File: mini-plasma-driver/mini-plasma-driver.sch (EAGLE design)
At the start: 73 parts, among them IC1 IR21844D, IC2 74LS19N, IC3 NE555N, IC4 NCP781IC, IC5 IR21844D, Q1 IRF640, Q2 IRF640, Q3 2N2369, Q4 2N2369, Q5 IRF640, Q6 IRF640

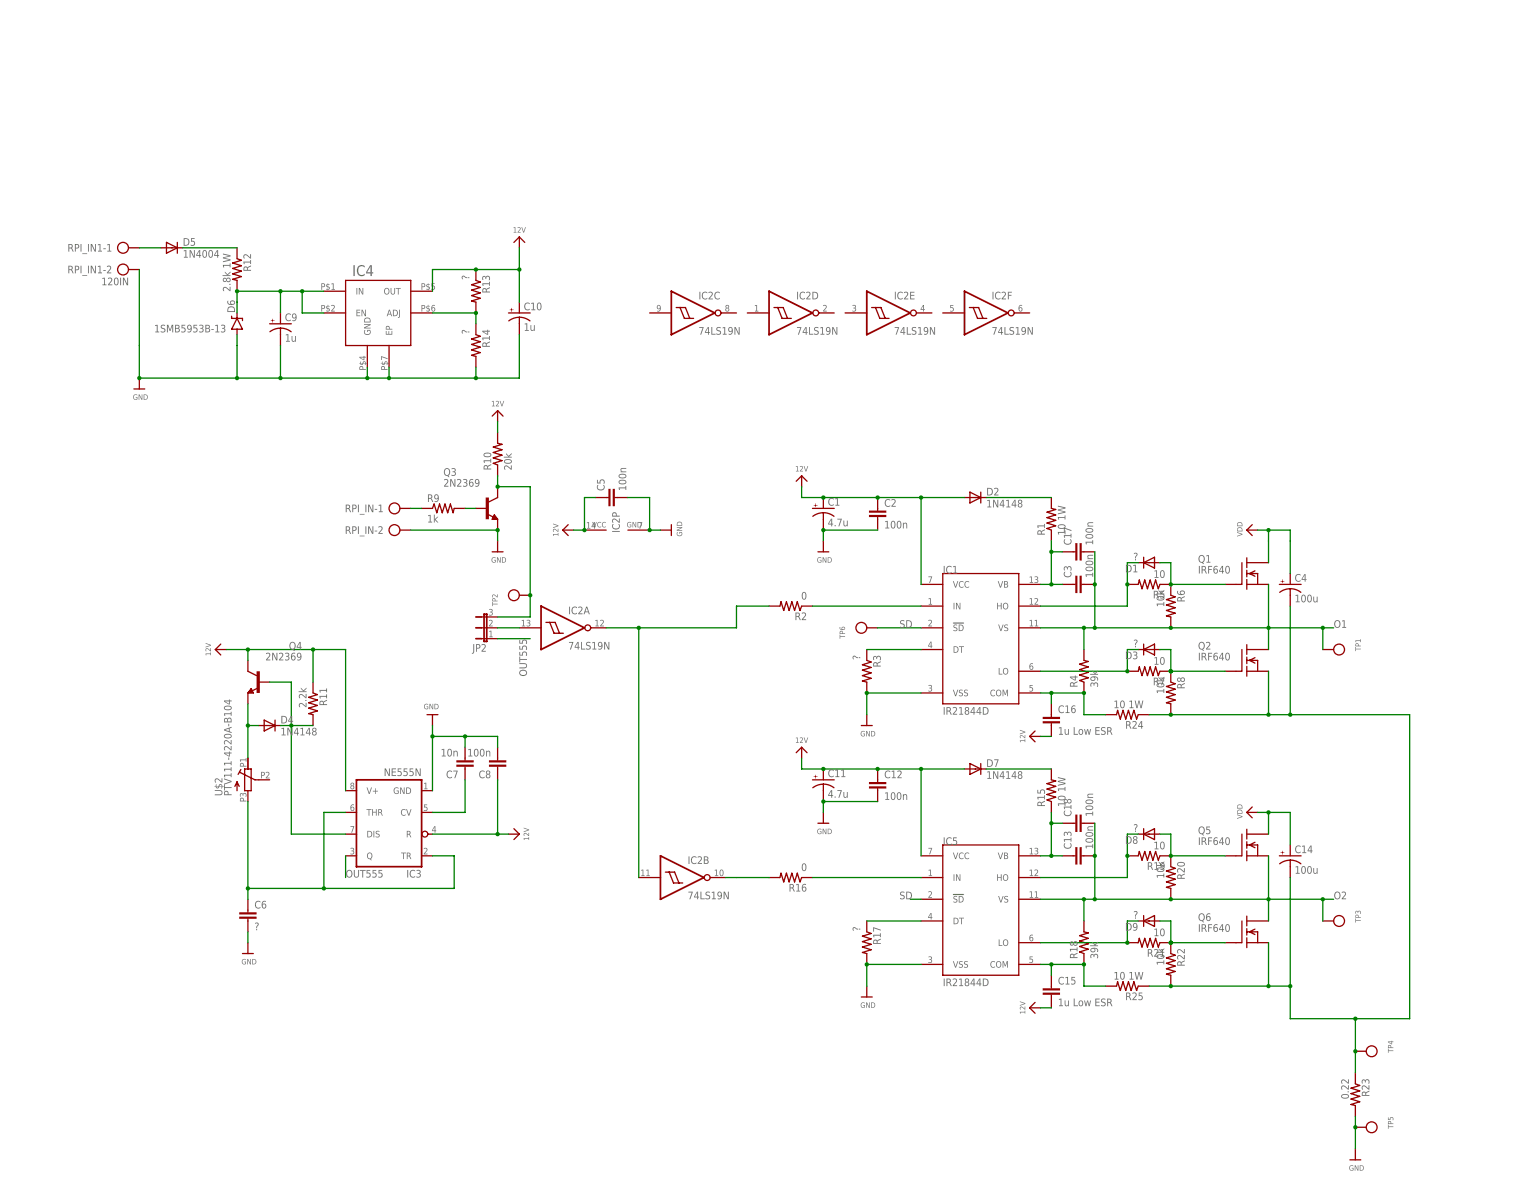
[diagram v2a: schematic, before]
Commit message: changed labels on AC connector and on 4 diodes
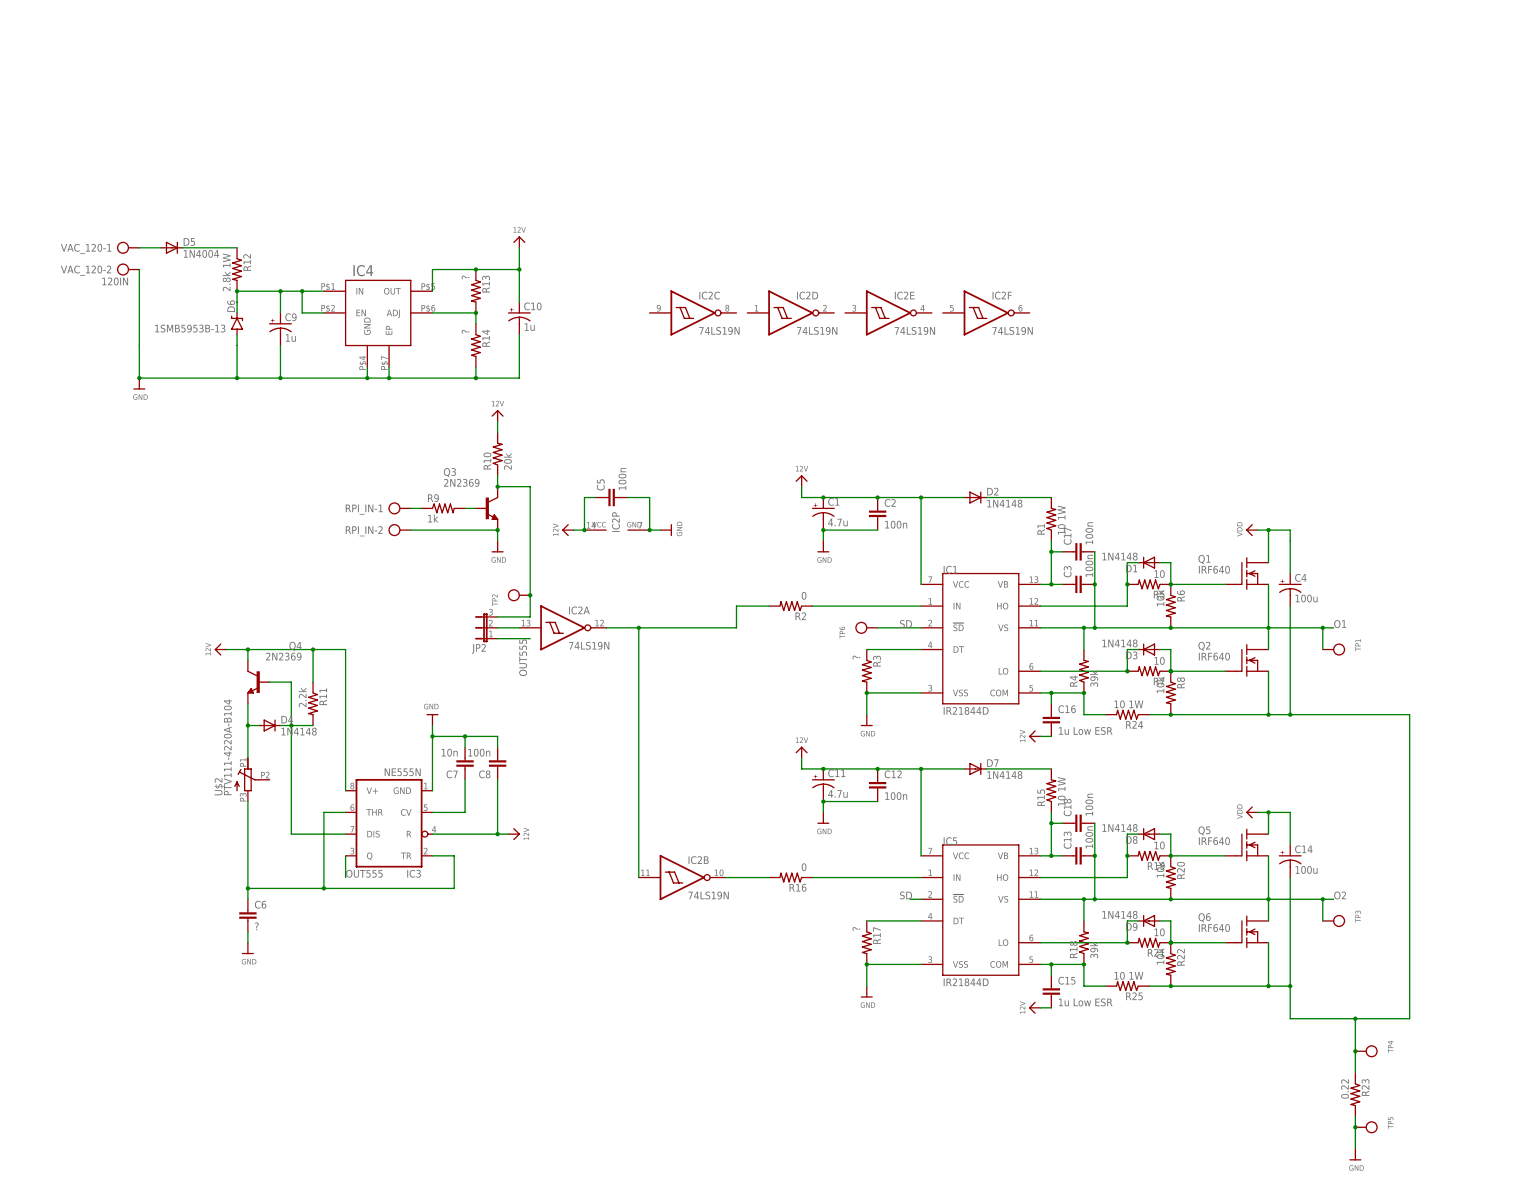
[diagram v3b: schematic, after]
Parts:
- D1, D3, D8, D9: value ? -> 1N4148
- renumbered RPI_IN1 to VAC_120
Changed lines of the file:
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@@
 <part name="R4" library="rcl" library_urn="urn:adsk.eagle:library:334" deviceset="R-US_" device="0207/10" package3d_urn="urn:adsk.eagle:package:23491/1" value="39k"/>
 <part name="D2" library="diode" library_urn="urn:adsk.eagle:library:210" deviceset="1N4148" device="DO35-10" package3d_urn="urn:adsk.eagle:package:43344/2" value="1N4148"/>
-<part name="D1" library="diode" library_urn="urn:adsk.eagle:library:210" deviceset="1N4148" device="DO35-10" package3d_urn="urn:adsk.eagle:package:43344/2" value="?"/>
+<part name="D1" library="diode" library_urn="urn:adsk.eagle:library:210" deviceset="1N4148" device="DO35-10" package3d_urn="urn:adsk.eagle:package:43344/2" value="1N4148"/>
 <part name="R5" library="rcl" library_urn="urn:adsk.eagle:library:334" deviceset="R-US_" device="0207/10" package3d_urn="urn:adsk.eagle:package:23491/1" value="10"/>
 <part name="R6" library="rcl" library_urn="urn:adsk.eagle:library:334" deviceset="R-US_" device="0207/10" package3d_urn="urn:adsk.eagle:package:23491/1" value="10k"/>
-<part name="D3" library="diode" library_urn="urn:adsk.eagle:library:210" deviceset="1N4148" device="DO35-10" package3d_urn="urn:adsk.eagle:package:43344/2" value="?"/>
+<part name="D3" library="diode" library_urn="urn:adsk.eagle:library:210" deviceset="1N4148" device="DO35-10" package3d_urn="urn:adsk.eagle:package:43344/2" value="1N4148"/>
 <part name="R7" library="rcl" library_urn="urn:adsk.eagle:library:334" deviceset="R-US_" device="0207/10" package3d_urn="urn:adsk.eagle:package:23491/1" value="10"/>
 <part name="R8" library="rcl" library_urn="urn:adsk.eagle:library:334" deviceset="R-US_" device="0207/10" package3d_urn="urn:adsk.eagle:package:23491/1" value="10k"/>
@@
 <part name="R12" library="rcl" library_urn="urn:adsk.eagle:library:334" deviceset="R-US_" device="0207/10" package3d_urn="urn:adsk.eagle:package:23491/1" value="2.8k 1W"/>
 <part name="D6" library="SparkFun-DiscreteSemi" deviceset="DIODE-ZENER" device="SMB" value="1SMB5953B-13"/>
-<part name="RPI_IN1" library="con-ptr500" library_urn="urn:adsk.eagle:library:181" deviceset="AK500/2" device="" package3d_urn="urn:adsk.eagle:package:9880/1" value="120IN"/>
+<part name="VAC_120" library="con-ptr500" library_urn="urn:adsk.eagle:library:181" deviceset="AK500/2" device="" package3d_urn="urn:adsk.eagle:package:9880/1" value="120IN"/>
 <part name="C9" library="rcl" library_urn="urn:adsk.eagle:library:334" deviceset="CPOL-US" device="E2.5-5" package3d_urn="urn:adsk.eagle:package:23344/1" value="1u"/>
 <part name="R13" library="rcl" library_urn="urn:adsk.eagle:library:334" deviceset="R-US_" device="0207/10" package3d_urn="urn:adsk.eagle:package:23491/1" value="?"/>
@@
 <part name="R18" library="rcl" library_urn="urn:adsk.eagle:library:334" deviceset="R-US_" device="0207/10" package3d_urn="urn:adsk.eagle:package:23491/1" value="39k"/>
 <part name="D7" library="diode" library_urn="urn:adsk.eagle:library:210" deviceset="1N4148" device="DO35-10" package3d_urn="urn:adsk.eagle:package:43344/2" value="1N4148"/>
-<part name="D8" library="diode" library_urn="urn:adsk.eagle:library:210" deviceset="1N4148" device="DO35-10" package3d_urn="urn:adsk.eagle:package:43344/2" value="?"/>
+<part name="D8" library="diode" library_urn="urn:adsk.eagle:library:210" deviceset="1N4148" device="DO35-10" package3d_urn="urn:adsk.eagle:package:43344/2" value="1N4148"/>
 <part name="R19" library="rcl" library_urn="urn:adsk.eagle:library:334" deviceset="R-US_" device="0207/10" package3d_urn="urn:adsk.eagle:package:23491/1" value="10"/>
 <part name="R20" library="rcl" library_urn="urn:adsk.eagle:library:334" deviceset="R-US_" device="0207/10" package3d_urn="urn:adsk.eagle:package:23491/1" value="10k"/>
-<part name="D9" library="diode" library_urn="urn:adsk.eagle:library:210" deviceset="1N4148" device="DO35-10" package3d_urn="urn:adsk.eagle:package:43344/2" value="?"/>
+<part name="D9" library="diode" library_urn="urn:adsk.eagle:library:210" deviceset="1N4148" device="DO35-10" package3d_urn="urn:adsk.eagle:package:43344/2" value="1N4148"/>
 <part name="R21" library="rcl" library_urn="urn:adsk.eagle:library:334" deviceset="R-US_" device="0207/10" package3d_urn="urn:adsk.eagle:package:23491/1" value="10"/>
 <part name="R22" library="rcl" library_urn="urn:adsk.eagle:library:334" deviceset="R-US_" device="0207/10" package3d_urn="urn:adsk.eagle:package:23491/1" value="10k"/>
@@
 <attribute name="VALUE" x="-63.5" y="119.1514" size="1.778" layer="96" rot="R180"/>
 </instance>
-<instance part="RPI_IN1" gate="-1" x="-88.9" y="137.16"/>
-<instance part="RPI_IN1" gate="-2" x="-88.9" y="132.08"/>
+<instance part="VAC_120" gate="-1" x="-88.9" y="137.16"/>
+<instance part="VAC_120" gate="-2" x="-88.9" y="132.08"/>
 <instance part="C9" gate="G$1" x="-50.8" y="119.38"/>
 <instance part="R13" gate="G$1" x="-5.08" y="127" rot="R270"/>
@@
 <pinref part="IC4" gate="G$1" pin="EP"/>
 <wire x1="-25.4" y1="109.22" x2="-25.4" y2="106.68" width="0.1524" layer="91"/>
-<pinref part="RPI_IN1" gate="-2" pin="KL"/>
+<pinref part="VAC_120" gate="-2" pin="KL"/>
 <wire x1="-83.82" y1="114.3" x2="-83.82" y2="132.08" width="0.1524" layer="91"/>
 <wire x1="-25.4" y1="106.68" x2="-30.48" y2="106.68" width="0.1524" layer="91"/>
@@
 <net name="N$18" class="0">
 <segment>
-<pinref part="RPI_IN1" gate="-1" pin="KL"/>
+<pinref part="VAC_120" gate="-1" pin="KL"/>
 <pinref part="D5" gate="1" pin="A"/>
 <wire x1="-83.82" y1="137.16" x2="-78.74" y2="137.16" width="0.1524" layer="91"/>

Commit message: changed diodes to MUR120, added connectors, fuse, LED on 12v
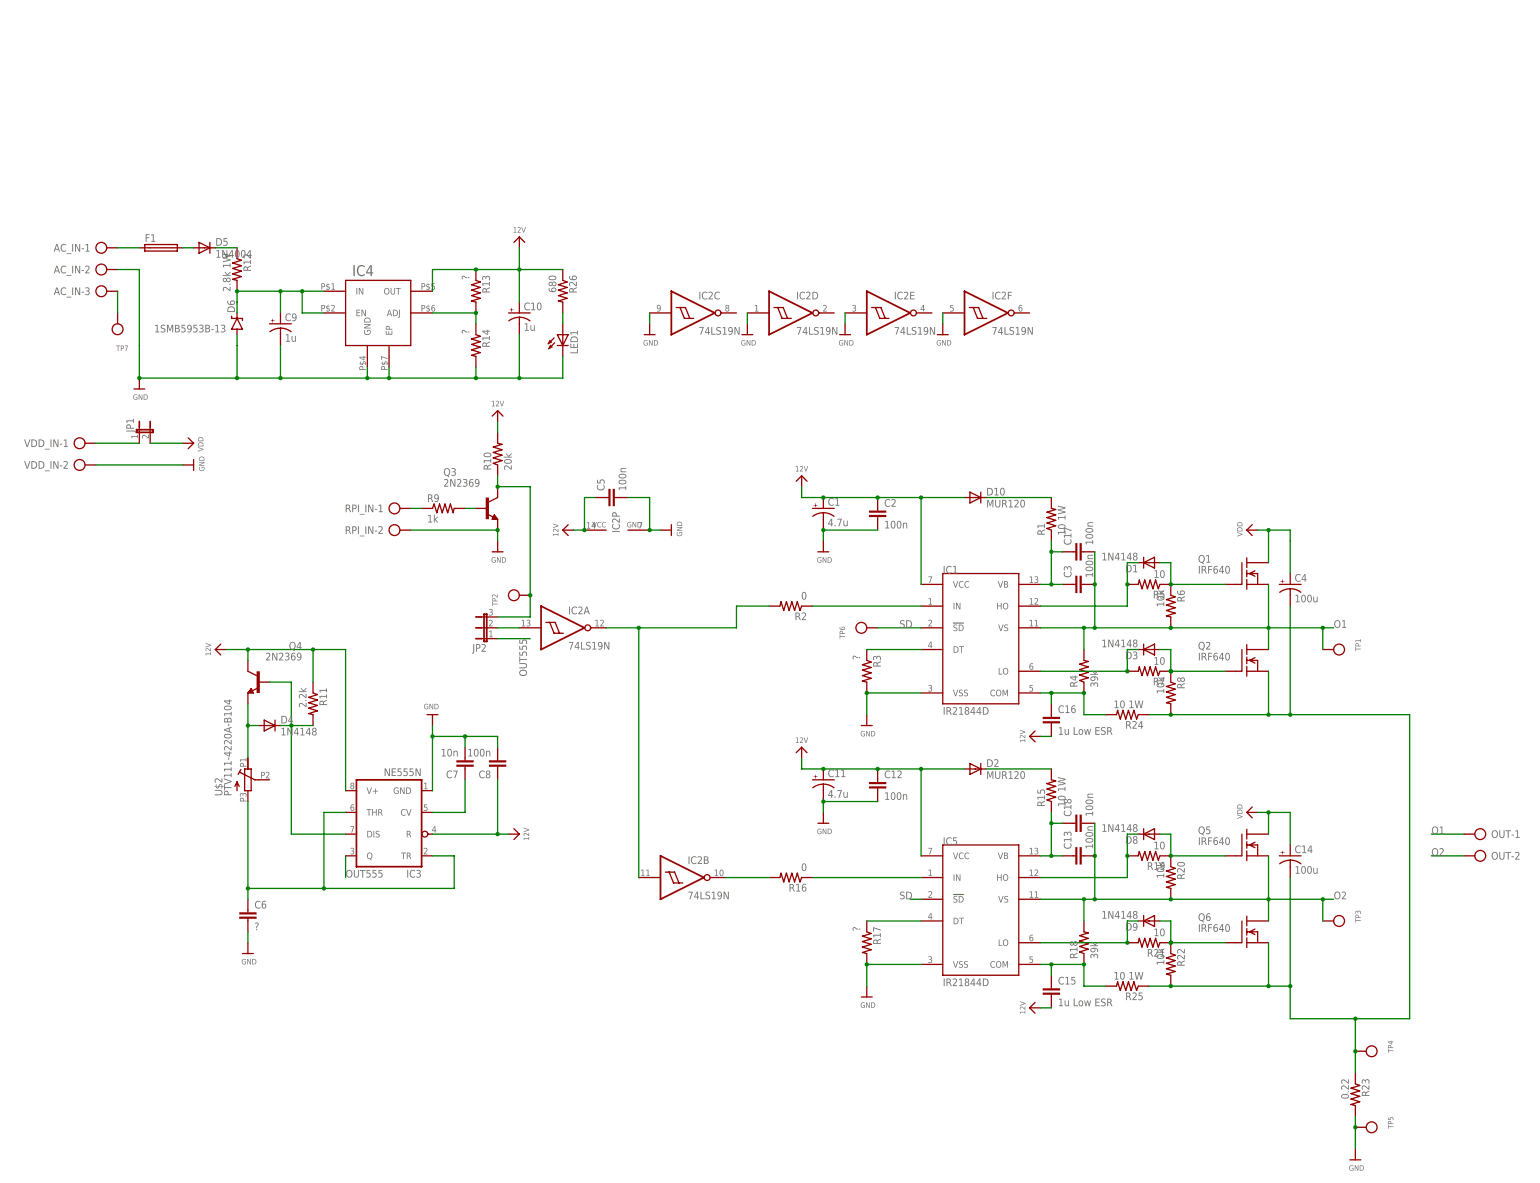
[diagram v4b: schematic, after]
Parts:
- removed D7: 1N4148, diode:1N4148DO35-10
- removed VAC_120: 120IN, con-ptr500:AK500/2
- added AC_IN: (no value), con-ptr500:AK500/3
- added D10: MUR120, diode:MUR150RL
- added F1: (no value), fuse:SH22,5A
- added JP1: (no value), jumper:JP1E
- added LED1: (no value), led:LED5MM
- added OUT, VDD_IN: (no value), con-ptr500:AK500/2
- added R26: 680, rcl:R-US_0207/10
- added TP7: (no value), microbuilder:TESTPOINT0.1"
- D2: value 1N4148 -> MUR120; device diode:1N4148DO35-10 -> diode:MUR150RL
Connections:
- new net N$25: AC_IN-3.KL, TP7.P$1
- new net N$31: AC_IN-1.KL, F1.1
- new net N$32: LED1.A, R26.2
- new net N$33: JP1.1, VDD_IN-1.KL
- net 12V: now also D10.A, R26.1; no longer D7.A
- net GND: now also AC_IN-2.KL, IC2C.I, IC2D.I, IC2E.I, IC2F.I, LED1.C, VDD_IN-2.KL; no longer VAC_120-2.KL
- net N$1: now also D10.C; no longer D2.C
- net N$18: now also F1.2; no longer VAC_120-1.KL
- net N$21: now also D2.C; no longer D7.C
- net O1: now also OUT-1.KL
- net O2: now also OUT-2.KL
- net VDD: now also JP1.2
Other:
- moved on the sheet: D5

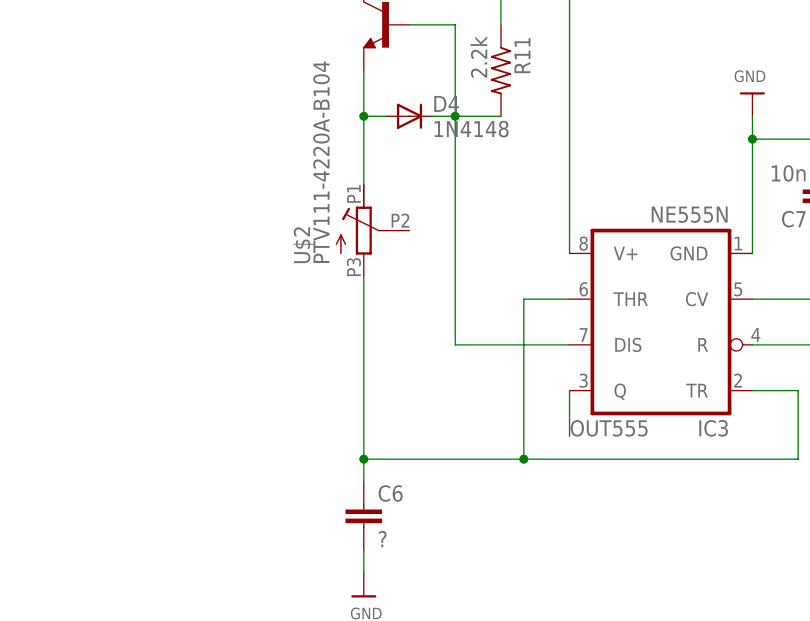
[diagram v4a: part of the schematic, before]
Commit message: moved TP2 to JP2 from JP3; connected P2 to P3 on trimpot; added TP at P1, P3 for possible off-board pot
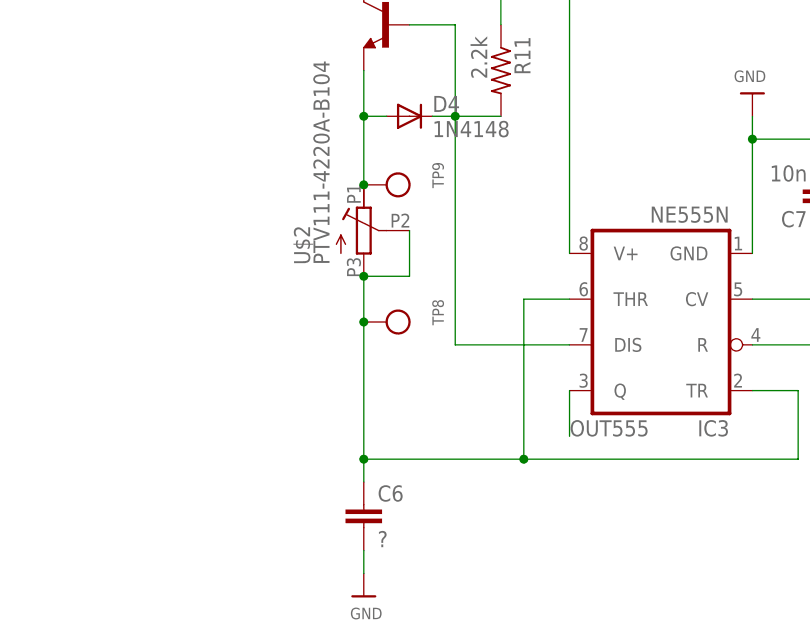
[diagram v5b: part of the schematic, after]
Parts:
- added TP8, TP9: (no value), microbuilder:TESTPOINT0.1"
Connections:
- net N$15: now also TP8.P$1, U$2.S
- net N$16: now also TP9.P$1
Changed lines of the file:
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@@
 <part name="U$4" library="microbuilder" deviceset="VDD" device=""/>
 <part name="GND15" library="microbuilder" deviceset="GND" device=""/>
+<part name="TP8" library="microbuilder" deviceset="TESTPOINT" device="0.1&quot;"/>
+<part name="TP9" library="microbuilder" deviceset="TESTPOINT" device="0.1&quot;"/>
 </parts>
 <sheets>
@@
 <instance part="U$4" gate="G$1" x="-71.12" y="91.44" rot="R270"/>
 <instance part="GND15" gate="G$1" x="-71.12" y="86.36" rot="R90"/>
+<instance part="TP8" gate="G$1" x="-58.42" y="2.54" rot="R270"/>
+<instance part="TP9" gate="G$1" x="-58.42" y="17.78" rot="R270"/>
 </instances>
 <busses>
@@
 <pinref part="U$2" gate="G$1" pin="A"/>
 <junction x="-58.42" y="25.4"/>
+<pinref part="TP9" gate="G$1" pin="P$1"/>
+<junction x="-58.42" y="17.78"/>
 </segment>
 </net>
@@
 <segment>
 <pinref part="U$2" gate="G$1" pin="E"/>
-<wire x1="-58.42" y1="-12.7" x2="-58.42" y2="7.62" width="0.1524" layer="91"/>
+<wire x1="-58.42" y1="-12.7" x2="-58.42" y2="2.54" width="0.1524" layer="91"/>
 <pinref part="IC3" gate="A" pin="THR"/>
+<wire x1="-58.42" y1="2.54" x2="-58.42" y2="7.62" width="0.1524" layer="91"/>
 <wire x1="-35.56" y1="5.08" x2="-40.64" y2="5.08" width="0.1524" layer="91"/>
 <wire x1="-40.64" y1="5.08" x2="-40.64" y2="-12.7" width="0.1524" layer="91"/>
@@
 <wire x1="-58.42" y1="-15.24" x2="-58.42" y2="-12.7" width="0.1524" layer="91"/>
 <junction x="-58.42" y="-12.7"/>
-</segment>
-</net>
+<pinref part="U$2" gate="G$1" pin="S"/>
+<wire x1="-53.34" y1="12.7" x2="-53.34" y2="7.62" width="0.1524" layer="91"/>
+<wire x1="-53.34" y1="7.62" x2="-58.42" y2="7.62" width="0.1524" layer="91"/>
+<junction x="-58.42" y="7.62"/>
+<pinref part="TP8" gate="G$1" pin="P$1"/>
+<junction x="-58.42" y="2.54"/>
+</segment>
+</net>
